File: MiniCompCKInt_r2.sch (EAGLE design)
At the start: 87 parts, among them IC2 74LS374N, IC3 74LS138N, IC4 74LS48N, IC5 74LS90N, IC6 74LS90N, Q1 BC547, Q2 BC547

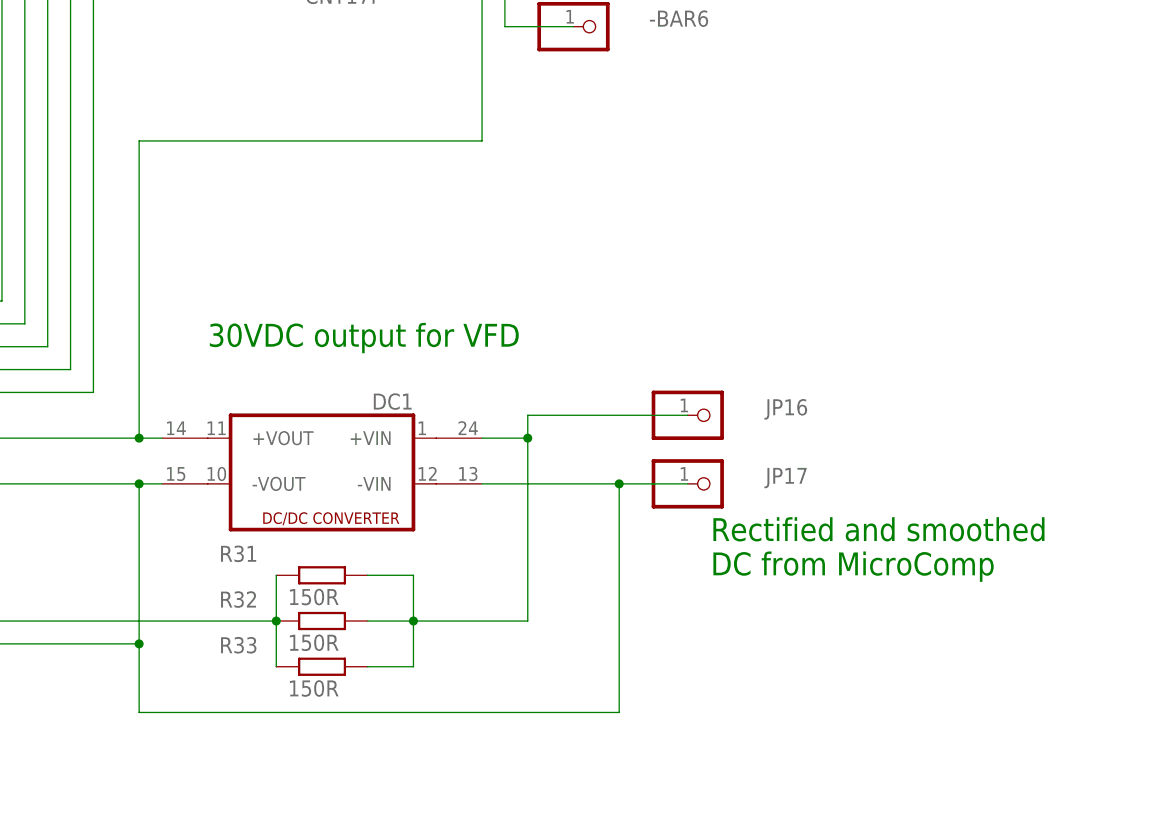
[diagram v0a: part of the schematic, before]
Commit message: Corrected error in VFD power supply circuit
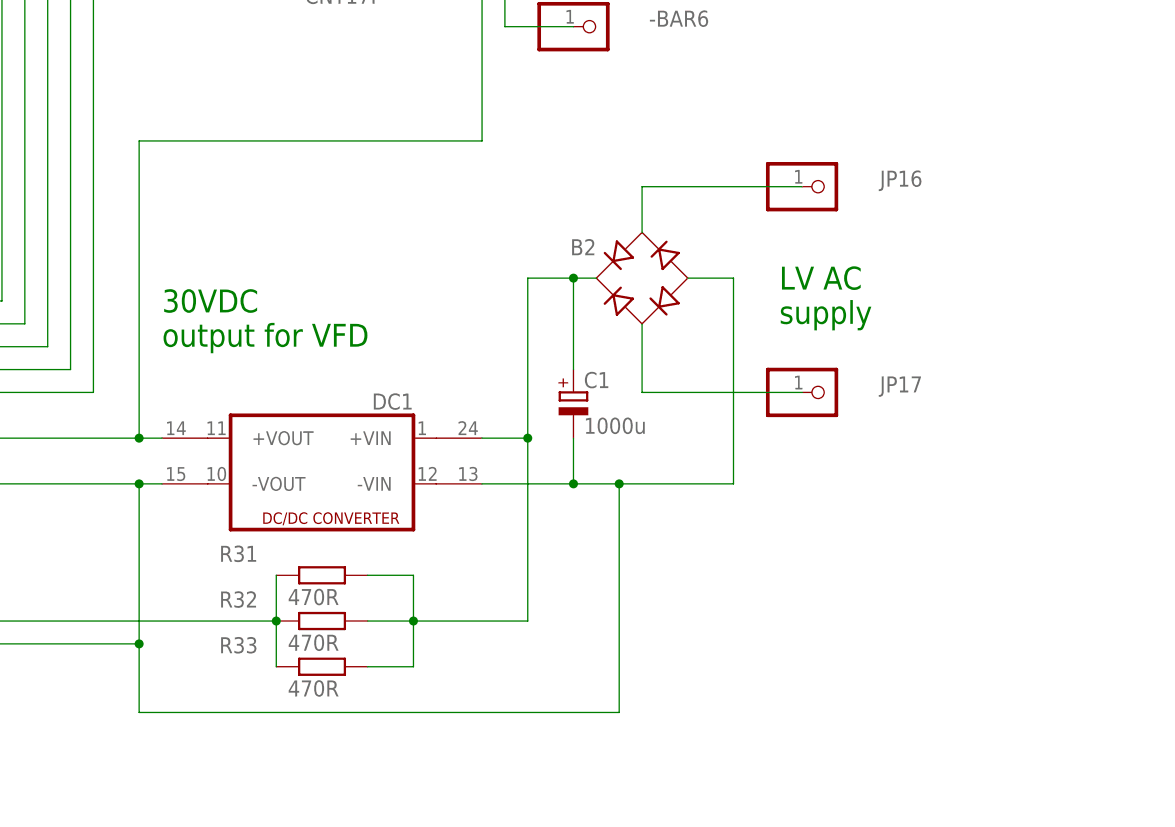
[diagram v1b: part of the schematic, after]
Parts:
- added B2: B1S, rectifier:B1S
- added C1: 1000u, resistor:CPOL-EUE3.5-10
- R31, R32, R33: value 150R -> 470R
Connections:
- new net N$82: B2.AC2, JP17.1
- new net N$87: B2.AC1, JP16.1
- net N$75: now also B2.-, C1.-; no longer JP17.1
- net N$83: now also B2.+, C1.+; no longer JP16.1
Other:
- note added: "LV AC supply"
- note removed: "Rectified and smoothed DC from MicroComp"
- moved on the sheet: JP16, JP17
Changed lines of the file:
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@@
 <part name="JP27" library="Connector" library_urn="urn:adsk.eagle:library:16378166" deviceset="PINHD-1X2" device="/90" package3d_urn="urn:adsk.eagle:package:22437/2"/>
 <part name="R28" library="resistor" library_urn="urn:adsk.eagle:library:348" deviceset="R-EU_" device="0204/7" value="100K"/>
-<part name="R31" library="resistor" library_urn="urn:adsk.eagle:library:348" deviceset="R-EU_" device="0204/7" value="150R"/>
-<part name="R32" library="resistor" library_urn="urn:adsk.eagle:library:348" deviceset="R-EU_" device="0204/7" value="150R"/>
-<part name="R33" library="resistor" library_urn="urn:adsk.eagle:library:348" deviceset="R-EU_" device="0204/7" value="150R"/>
+<part name="R31" library="resistor" library_urn="urn:adsk.eagle:library:348" deviceset="R-EU_" device="0204/7" value="470R"/>
+<part name="R32" library="resistor" library_urn="urn:adsk.eagle:library:348" deviceset="R-EU_" device="0204/7" value="470R"/>
+<part name="R33" library="resistor" library_urn="urn:adsk.eagle:library:348" deviceset="R-EU_" device="0204/7" value="470R"/>
+<part name="B2" library="rectifier" library_urn="urn:adsk.eagle:library:336" deviceset="B*S" device="" package3d_urn="urn:adsk.eagle:package:23901/1" technology="1"/>
+<part name="C1" library="resistor" library_urn="urn:adsk.eagle:library:348" deviceset="CPOL-EU" device="E3.5-10" value="1000u"/>
 </parts>
 <sheets>
@@
 <text x="-86.36" y="-68.58" size="5.08" layer="91">Latch and decode board</text>
 <text x="109.22" y="-68.58" size="5.08" layer="91">VFD driver board</text>
-<text x="198.12" y="-20.32" size="2.54" layer="91">30VDC output for VFD</text>
+<text x="193.04" y="-20.32" size="2.54" layer="91">30VDC
+output for VFD</text>
 <text x="162.56" y="-55.88" size="2.54" layer="91" align="bottom-right">VFD filiment
 drive</text>
-<text x="254" y="-45.72" size="2.54" layer="91">Rectified and smoothed
-DC from MicroComp</text>
+<text x="261.62" y="-17.78" size="2.54" layer="91">LV AC
+supply </text>
 </plain>
 <instances>
@@
 <attribute name="VALUE" x="220.98" y="-43.18" size="1.778" layer="96" rot="MR0"/>
 </instance>
-<instance part="JP16" gate="G$1" x="254" y="-27.94" smashed="yes">
-<attribute name="NAME" x="260.096" y="-27.94" size="1.778" layer="95"/>
-<attribute name="VALUE" x="247.65" y="-33.02" size="1.778" layer="96" display="off"/>
-</instance>
-<instance part="JP17" gate="G$1" x="254" y="-35.56" smashed="yes">
-<attribute name="NAME" x="260.096" y="-35.56" size="1.778" layer="95"/>
-<attribute name="VALUE" x="247.65" y="-40.64" size="1.778" layer="96" display="off"/>
+<instance part="JP16" gate="G$1" x="266.7" y="-2.54" smashed="yes">
+<attribute name="NAME" x="272.796" y="-2.54" size="1.778" layer="95"/>
+<attribute name="VALUE" x="260.35" y="-7.62" size="1.778" layer="96" display="off"/>
+</instance>
+<instance part="JP17" gate="G$1" x="266.7" y="-25.4" smashed="yes">
+<attribute name="NAME" x="272.796" y="-25.4" size="1.778" layer="95"/>
+<attribute name="VALUE" x="260.35" y="-30.48" size="1.778" layer="96" display="off"/>
 </instance>
 <instance part="Q2" gate="G$1" x="76.2" y="10.16" smashed="yes">
@@
 <attribute name="NAME" x="199.39" y="-54.3814" size="1.778" layer="95"/>
 <attribute name="VALUE" x="207.01" y="-59.182" size="1.778" layer="96"/>
+</instance>
+<instance part="B2" gate="G$1" x="246.38" y="-12.7" smashed="yes" rot="MR0">
+<attribute name="VALUE" x="241.3" y="-17.78" size="1.778" layer="96" rot="MR0" display="off"/>
+<attribute name="NAME" x="241.3" y="-10.16" size="1.778" layer="95" rot="MR0"/>
+</instance>
+<instance part="C1" gate="G$1" x="238.76" y="-25.4" smashed="yes">
+<attribute name="NAME" x="239.903" y="-24.9174" size="1.778" layer="95"/>
+<attribute name="VALUE" x="239.903" y="-29.9974" size="1.778" layer="96"/>
 </instance>
 </instances>
@@
 <junction x="190.5" y="-53.34"/>
 <junction x="190.5" y="-35.56"/>
-<pinref part="JP17" gate="G$1" pin="1"/>
+<wire x1="190.5" y1="-60.96" x2="243.84" y2="-60.96" width="0.1524" layer="91"/>
 <pinref part="DC1" gate="G$1" pin="-VIN1"/>
-<wire x1="251.46" y1="-35.56" x2="243.84" y2="-35.56" width="0.1524" layer="91"/>
-<wire x1="243.84" y1="-35.56" x2="228.6" y2="-35.56" width="0.1524" layer="91"/>
-<wire x1="190.5" y1="-60.96" x2="243.84" y2="-60.96" width="0.1524" layer="91"/>
+<wire x1="228.6" y1="-35.56" x2="238.76" y2="-35.56" width="0.1524" layer="91"/>
+<pinref part="B2" gate="G$1" pin="-"/>
+<wire x1="238.76" y1="-35.56" x2="243.84" y2="-35.56" width="0.1524" layer="91"/>
+<wire x1="243.84" y1="-35.56" x2="256.54" y2="-35.56" width="0.1524" layer="91"/>
+<wire x1="256.54" y1="-35.56" x2="256.54" y2="-12.7" width="0.1524" layer="91"/>
+<wire x1="256.54" y1="-12.7" x2="251.46" y2="-12.7" width="0.1524" layer="91"/>
+<pinref part="C1" gate="G$1" pin="-"/>
+<wire x1="238.76" y1="-30.48" x2="238.76" y2="-35.56" width="0.1524" layer="91"/>
+<junction x="238.76" y="-35.56"/>
 <wire x1="243.84" y1="-60.96" x2="243.84" y2="-35.56" width="0.1524" layer="91"/>
 <junction x="243.84" y="-35.56"/>
@@
 <net name="N$83" class="0">
 <segment>
-<pinref part="JP16" gate="G$1" pin="1"/>
 <pinref part="DC1" gate="G$1" pin="+VIN1"/>
 <wire x1="228.6" y1="-30.48" x2="233.68" y2="-30.48" width="0.1524" layer="91"/>
-<wire x1="233.68" y1="-30.48" x2="233.68" y2="-27.94" width="0.1524" layer="91"/>
-<wire x1="233.68" y1="-27.94" x2="251.46" y2="-27.94" width="0.1524" layer="91"/>
 <wire x1="233.68" y1="-30.48" x2="233.68" y2="-50.8" width="0.1524" layer="91"/>
 <wire x1="233.68" y1="-50.8" x2="220.98" y2="-50.8" width="0.1524" layer="91"/>
@@
 <junction x="233.68" y="-30.48"/>
 <junction x="220.98" y="-50.8"/>
+<wire x1="233.68" y1="-30.48" x2="233.68" y2="-12.7" width="0.1524" layer="91"/>
+<pinref part="B2" gate="G$1" pin="+"/>
+<wire x1="233.68" y1="-12.7" x2="238.76" y2="-12.7" width="0.1524" layer="91"/>
+<pinref part="C1" gate="G$1" pin="+"/>
+<wire x1="238.76" y1="-12.7" x2="241.3" y2="-12.7" width="0.1524" layer="91"/>
+<wire x1="238.76" y1="-22.86" x2="238.76" y2="-12.7" width="0.1524" layer="91"/>
+<junction x="238.76" y="-12.7"/>
 </segment>
 </net>
@@
 </segment>
 </net>
+<net name="N$82" class="0">
+<segment>
+<pinref part="B2" gate="G$1" pin="AC2"/>
+<wire x1="246.38" y1="-17.78" x2="246.38" y2="-25.4" width="0.1524" layer="91"/>
+<pinref part="JP17" gate="G$1" pin="1"/>
+<wire x1="246.38" y1="-25.4" x2="264.16" y2="-25.4" width="0.1524" layer="91"/>
+</segment>
+</net>
+<net name="N$87" class="0">
+<segment>
+<pinref part="B2" gate="G$1" pin="AC1"/>
+<wire x1="246.38" y1="-7.62" x2="246.38" y2="-2.54" width="0.1524" layer="91"/>
+<pinref part="JP16" gate="G$1" pin="1"/>
+<wire x1="246.38" y1="-2.54" x2="264.16" y2="-2.54" width="0.1524" layer="91"/>
+</segment>
+</net>
